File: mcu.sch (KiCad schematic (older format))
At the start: 74 parts, among them J10 JTAG, J11 esp32L, J12 esp32B, J13 esp32R, J2 SPI1, J3 uSD, J4 I2C1, J5 serial1, J6 serial2, J7 touch interface, J8 LCD 4.3, J9 EXT_IOS, Q1 ZXMN2F30FH, Q2 ZXMN2F30FH, Q3 ZXMN2F30FH, SW1 reset, SW7 on, U3 AT25SF641, U5 STM32F750Z8, U6 MP3302DJ-LF-P, U7 ESP32-WROOM-32, Y1 25MHz, Y2 32.768 kHz

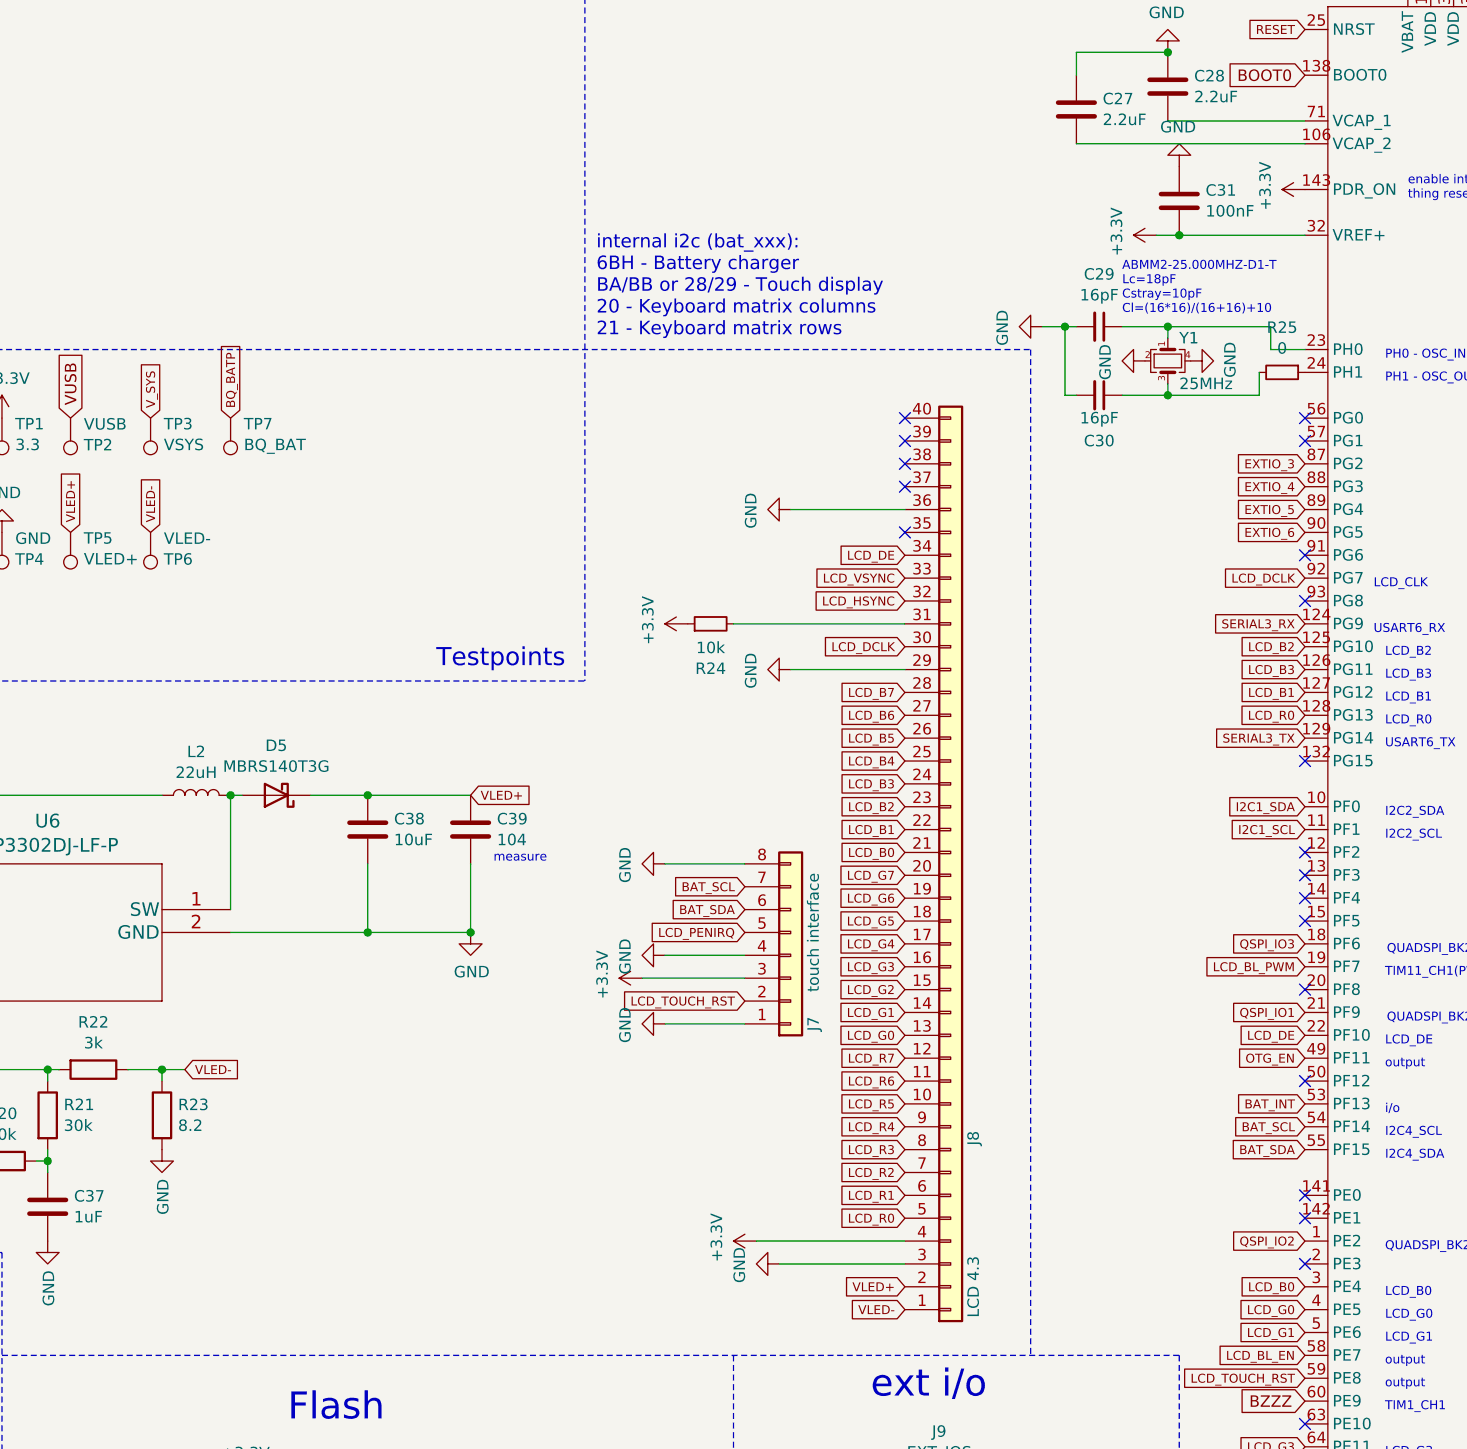
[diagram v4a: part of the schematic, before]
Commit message: Move touchscreen to user i2c with jumpers
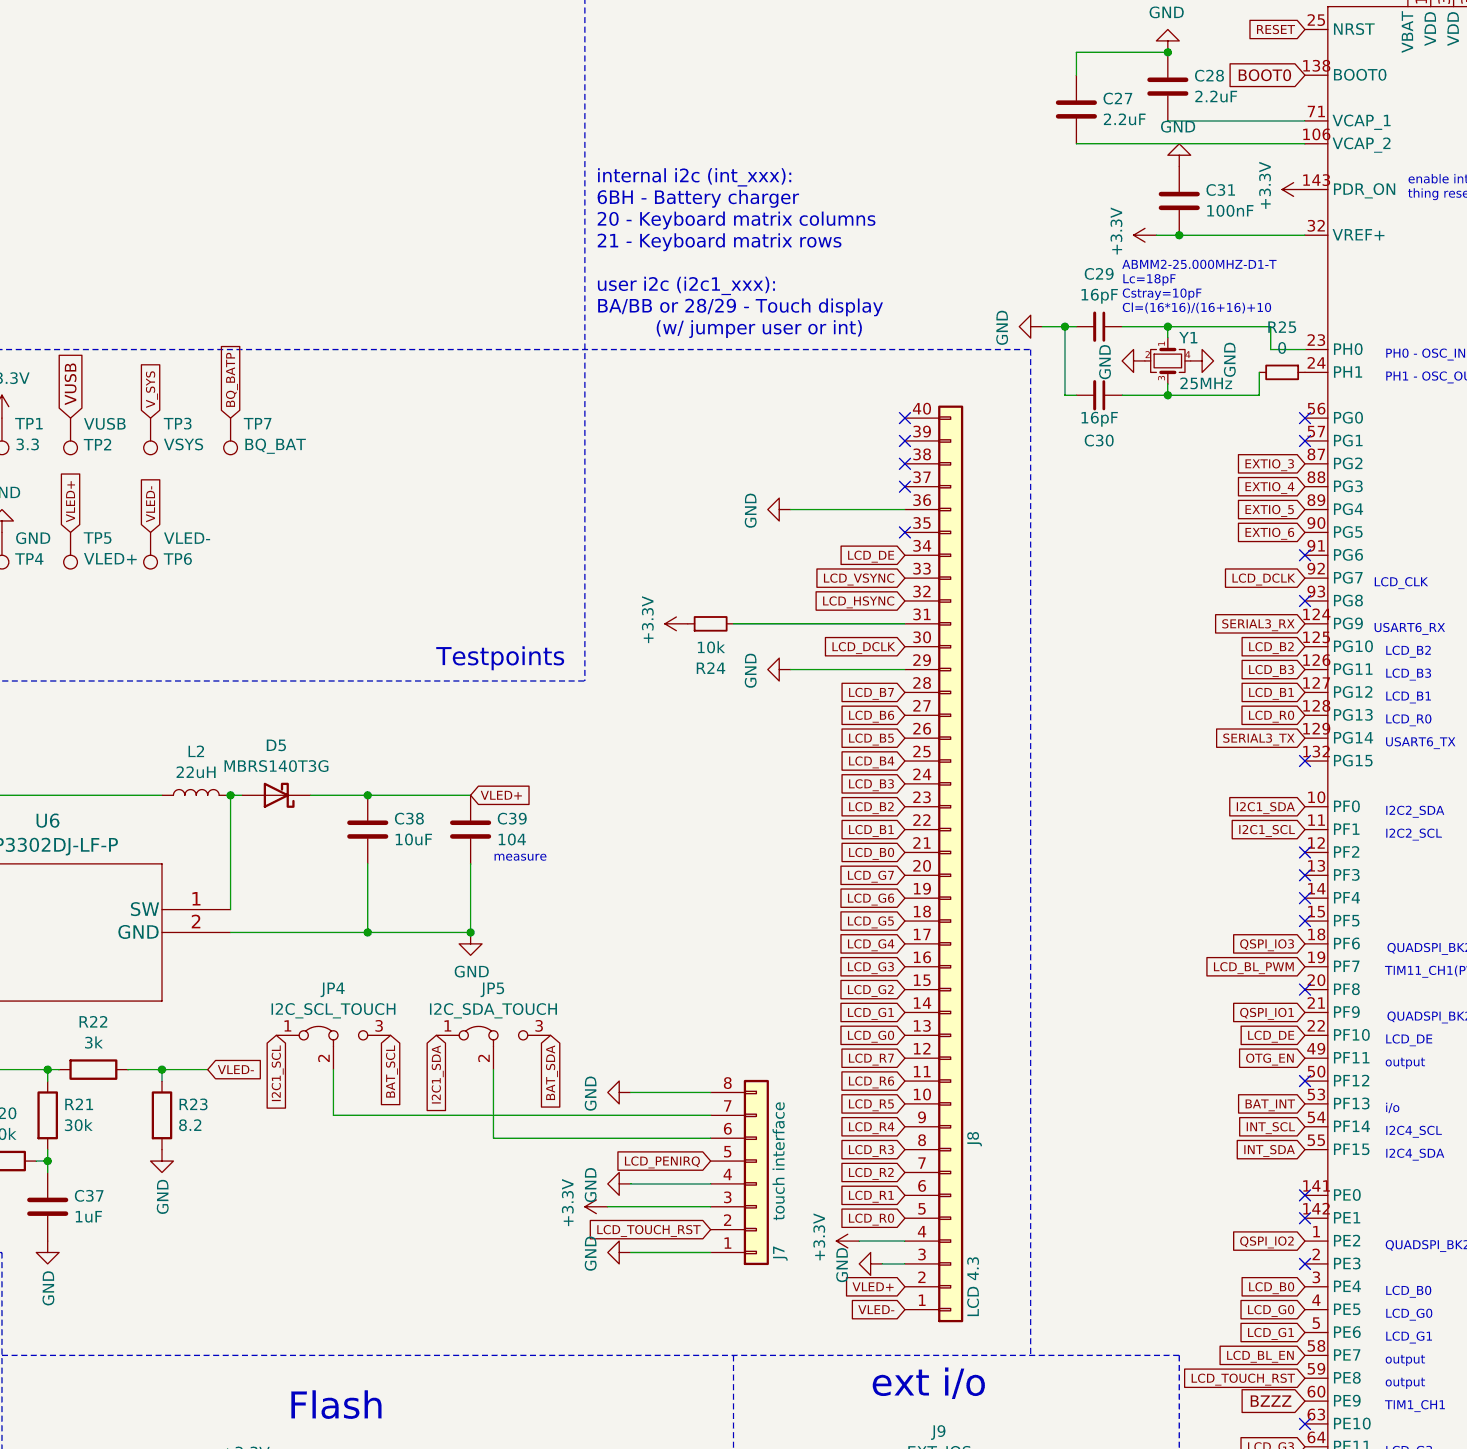
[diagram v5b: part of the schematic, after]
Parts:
- added JP4: I2C_SCL_TOUCH, Jumper:SolderJumper-3_P1.3mm_Bridged2Bar12_Pad1.0x1.5mm_NumberLabels, symbol Jumper:Jumper_3_Bridged12
- added JP5: I2C_SDA_TOUCH, Jumper:SolderJumper-3_P1.3mm_Bridged2Bar12_Pad1.0x1.5mm_NumberLabels, symbol Jumper:Jumper_3_Bridged12
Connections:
- net BAT_SCL: now also JP4.3 (B); no longer J7.7 (Pin_7), U5.54 (PF14)
- net BAT_SDA: now also JP5.3 (B); no longer J7.6 (Pin_6), U5.55 (PF15)
- net I2C1_SCL: now also JP4.1 (A)
- net I2C1_SDA: now also JP5.1 (A)
- new net: J7.6 (Pin_6), JP5.2 (C)
- new net: J7.7 (Pin_7), JP4.2 (C)
- new net INT_SCL: U5.54 (PF14)
- new net INT_SDA: U5.55 (PF15)
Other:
- note added: "internal i2c (int_xxx):\n6BH - Battery charger\n20 - Keyboard matrix columns\n21 - Keyboard matrix rows\n\nuser i2c (i2c1_xxx):\nBA/BB or 28/29 - Touch display\n (w/ jumper user or int)"
- note removed: "internal i2c (bat_xxx):\n6BH - Battery charger\nBA/BB or 28/29 - Touch display\n20 - Keyboard matrix columns\n21 - Keyboard matrix rows"
- moved on the sheet: J7
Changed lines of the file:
@@
 Text GLabel 15050 3150 2    50   Input ~ 0
 USB0_ID
-Text GLabel 10300 6100 0    39   Input ~ 0
+Text GLabel 10150 7100 0    39   Input ~ 0
 LCD_PENIRQ
 Text GLabel 11000 7350 0    39   Input ~ 0
@@
 Text GLabel 11000 4450 0    39   Input ~ 0
 LCD_DE
-Text GLabel 10300 6400 0    39   Input ~ 0
+Text GLabel 10150 7400 0    39   Input ~ 0
 LCD_TOUCH_RST
 Text GLabel 11000 6650 0    39   Input ~ 0
@@
 L power:GND #PWR0112
 U 1 1 5F98FFD8
-P 9950 6500
-F 0 "#PWR0112" H 9950 6250 50  0001 C CNN
-F 1 "GND" H 9955 6327 50  0000 C CNN
-F 2 "" H 9950 6500 50  0001 C CNN
-F 3 "" H 9950 6500 50  0001 C CNN
-	1    9950 6500
+P 9800 7500
+F 0 "#PWR0112" H 9800 7250 50  0001 C CNN
+F 1 "GND" H 9805 7327 50  0000 C CNN
+F 2 "" H 9800 7500 50  0001 C CNN
+F 3 "" H 9800 7500 50  0001 C CNN
+	1    9800 7500
 	0    1    1    0
 $EndComp
@@
 JTDO
 Text GLabel 12750 7050 0    39   Input ~ 0
-BAT_SDA
+INT_SDA
 Text GLabel 12750 6950 0    39   Input ~ 0
-BAT_SCL
+INT_SCL
 Text GLabel 12750 6850 0    39   Input ~ 0
 BAT_INT
@@
 L power:GND #PWR022
 U 1 1 60511AFC
-P 10450 7550
-F 0 "#PWR022" H 10450 7300 50  0001 C CNN
-F 1 "GND" H 10455 7377 50  0000 C CNN
-F 2 "" H 10450 7550 50  0001 C CNN
-F 3 "" H 10450 7550 50  0001 C CNN
-	1    10450 7550
-	0    1    1    0
-$EndComp
-Wire Wire Line
-	10450 7550 11000 7550
+P 10900 7550
+F 0 "#PWR022" H 10900 7300 50  0001 C CNN
+F 1 "GND" H 10905 7377 50  0000 C CNN
+F 2 "" H 10900 7550 50  0001 C CNN
+F 3 "" H 10900 7550 50  0001 C CNN
+	1    10900 7550
+	0    1    1    0
+$EndComp
+Wire Wire Line
+	10900 7550 11000 7550
 $Comp
 L power:+3.3V #PWR021
 U 1 1 6051DAFC
-P 10350 7450
-F 0 "#PWR021" H 10350 7300 50  0001 C CNN
-F 1 "+3.3V" H 10365 7623 50  0000 C CNN
-F 2 "" H 10350 7450 50  0001 C CNN
-F 3 "" H 10350 7450 50  0001 C CNN
-	1    10350 7450
+P 10800 7450
+F 0 "#PWR021" H 10800 7300 50  0001 C CNN
+F 1 "+3.3V" H 10815 7623 50  0000 C CNN
+F 2 "" H 10800 7450 50  0001 C CNN
+F 3 "" H 10800 7450 50  0001 C CNN
+	1    10800 7450
 	0    -1   -1   0
 $EndComp
 Wire Wire Line
-	10350 7450 11000 7450
+	10800 7450 11000 7450
 $Comp
 L power:GND #PWR026
@@
 L Connector_Generic:Conn_01x08 J7
 U 1 1 605D39D8
-P 10500 6200
-F 0 "J7" V 10600 6500 50  0000 C CNN
-F 1 "touch interface" V 10600 6100 50  0000 C CNN
-F 2 "Connector_FFC-FPC:TE_0-1734839-8_1x08-1MP_P0.5mm_Horizontal" H 10500 6200 50  0001 C CNN
-F 3 "~" H 10500 6200 50  0001 C CNN
-	1    10500 6200
+P 10350 7200
+F 0 "J7" V 10450 7500 50  0000 C CNN
+F 1 "touch interface" V 10450 7100 50  0000 C CNN
+F 2 "Connector_FFC-FPC:TE_0-1734839-8_1x08-1MP_P0.5mm_Horizontal" H 10350 7200 50  0001 C CNN
+F 3 "~" H 10350 7200 50  0001 C CNN
+	1    10350 7200
 	1    0    0    1
 $EndComp
@@
 L power:+3.3V #PWR016
 U 1 1 605D4C62
-P 9850 6300
-F 0 "#PWR016" H 9850 6150 50  0001 C CNN
-F 1 "+3.3V" H 9865 6473 50  0000 C CNN
-F 2 "" H 9850 6300 50  0001 C CNN
-F 3 "" H 9850 6300 50  0001 C CNN
-	1    9850 6300
+P 9700 7300
+F 0 "#PWR016" H 9700 7150 50  0001 C CNN
+F 1 "+3.3V" H 9715 7473 50  0000 C CNN
+F 2 "" H 9700 7300 50  0001 C CNN
+F 3 "" H 9700 7300 50  0001 C CNN
+	1    9700 7300
 	0    -1   -1   0
 $EndComp
@@
 L power:GND #PWR019
 U 1 1 605D5342
-P 9950 6200
-F 0 "#PWR019" H 9950 5950 50  0001 C CNN
-F 1 "GND" H 9955 6027 50  0000 C CNN
-F 2 "" H 9950 6200 50  0001 C CNN
-F 3 "" H 9950 6200 50  0001 C CNN
-	1    9950 6200
+P 9800 7200
+F 0 "#PWR019" H 9800 6950 50  0001 C CNN
+F 1 "GND" H 9805 7027 50  0000 C CNN
+F 2 "" H 9800 7200 50  0001 C CNN
+F 3 "" H 9800 7200 50  0001 C CNN
+	1    9800 7200
 	0    1    1    0
 $EndComp
 NoConn ~ 12750 6350
-Text GLabel 10300 5900 0    39   Input ~ 0
-BAT_SCL
-Text GLabel 10300 6000 0    39   Input ~ 0
-BAT_SDA
+Text GLabel 8250 6550 3    39   Input ~ 0
+I2C1_SCL
+Text GLabel 8950 6550 3    39   Input ~ 0
+I2C1_SDA
 $Comp
 L power:GND #PWR018
 U 1 1 6061D658
-P 9950 5800
-F 0 "#PWR018" H 9950 5550 50  0001 C CNN
-F 1 "GND" H 9955 5627 50  0000 C CNN
-F 2 "" H 9950 5800 50  0001 C CNN
-F 3 "" H 9950 5800 50  0001 C CNN
-	1    9950 5800
-	0    1    1    0
-$EndComp
-Wire Wire Line
-	9950 5800 10300 5800
-Wire Wire Line
-	10300 6500 9950 6500
-Wire Wire Line
-	9950 6200 10300 6200
-Wire Wire Line
-	10300 6300 9850 6300
+P 9800 6800
+F 0 "#PWR018" H 9800 6550 50  0001 C CNN
+F 1 "GND" H 9805 6627 50  0000 C CNN
+F 2 "" H 9800 6800 50  0001 C CNN
+F 3 "" H 9800 6800 50  0001 C CNN
+	1    9800 6800
+	0    1    1    0
+$EndComp
+Wire Wire Line
+	9800 6800 10150 6800
+Wire Wire Line
+	10150 7500 9800 7500
+Wire Wire Line
+	9800 7200 10150 7200
+Wire Wire Line
+	10150 7300 9700 7300
 $Comp
 L d_mps:MP3302DJ-LF-P U6
@@
 Text GLabel 11000 7650 0    39   Input ~ 0
 VLED+
-Text GLabel 7850 6700 2    39   Input ~ 0
+Text GLabel 7950 6700 2    39   Input ~ 0
 VLED-
 Wire Wire Line
-	7850 6700 7750 6700
+	7950 6700 7750 6700
 Wire Wire Line
 	7750 6700 7750 6750
@@
 KB_WAKEUP
 Text Notes 9650 3500 0    59   ~ 0
-internal i2c (bat_xxx):\n6BH - Battery charger\nBA/BB or 28/29 - Touch display\n20 - Keyboard matrix columns\n21 - Keyboard matrix rows
+internal i2c (int_xxx):\n6BH - Battery charger\n20 - Keyboard matrix columns\n21 - Keyboard matrix rows\n\nuser i2c (i2c1_xxx):\nBA/BB or 28/29 - Touch display\n          (w/ jumper user or int)
 $Comp
 L power:+3.3V #PWR0111
@@
 Wire Wire Line
 	6250 6000 5900 6000
+$Comp
+L Jumper:Jumper_3_Bridged12 JP4
+U 1 1 6188C10F
+P 8500 6550
+F 0 "JP4" H 8500 6754 50  0000 C CNN
+F 1 "I2C_SCL_TOUCH" H 8500 6663 50  0000 C CNN
+F 2 "Jumper:SolderJumper-3_P1.3mm_Bridged2Bar12_Pad1.0x1.5mm_NumberLabels" H 8500 6550 50  0001 C CNN
+F 3 "~" H 8500 6550 50  0001 C CNN
+	1    8500 6550
+	1    0    0    -1
+$EndComp
+$Comp
+L Jumper:Jumper_3_Bridged12 JP5
+U 1 1 6188CE27
+P 9200 6550
+F 0 "JP5" H 9200 6754 50  0000 C CNN
+F 1 "I2C_SDA_TOUCH" H 9200 6663 50  0000 C CNN
+F 2 "Jumper:SolderJumper-3_P1.3mm_Bridged2Bar12_Pad1.0x1.5mm_NumberLabels" H 9200 6550 50  0001 C CNN
+F 3 "~" H 9200 6550 50  0001 C CNN
+	1    9200 6550
+	1    0    0    -1
+$EndComp
+Wire Wire Line
+	8500 6700 8500 6900
+Wire Wire Line
+	8500 6900 10150 6900
+Wire Wire Line
+	9200 6700 9200 7000
+Wire Wire Line
+	9200 7000 10150 7000
+Text GLabel 8750 6550 3    39   Input ~ 0
+BAT_SCL
+Text GLabel 9450 6550 3    39   Input ~ 0
+BAT_SDA
 $EndSCHEMATC
